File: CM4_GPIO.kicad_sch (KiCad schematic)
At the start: 21 parts, among them J4 Conn_02x07_Odd_Even, J5 Conn_01x03, J6 Conn_01x03, J7 THD-20-R, J8 Micro_SD_Card_Det, U4 74LVC1G07SE-7, U5 74LVC1G07SE-7, U6 RT9742GGJ5

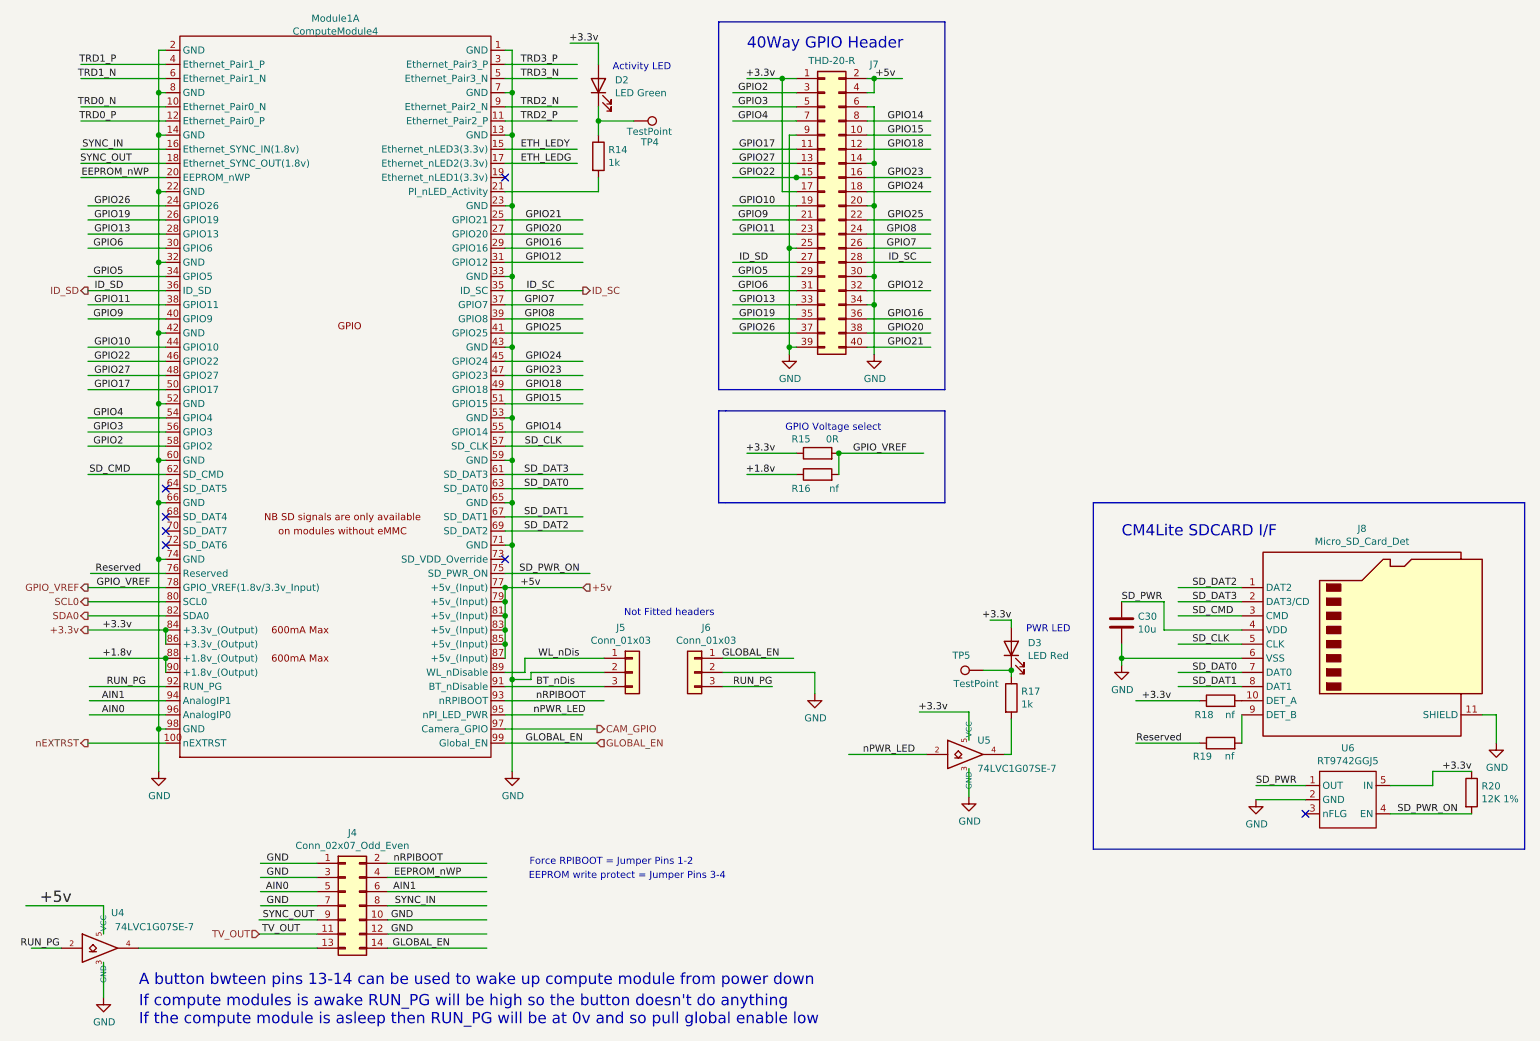
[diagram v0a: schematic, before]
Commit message: Initial layout and all parts added. Some pins still not connected to power
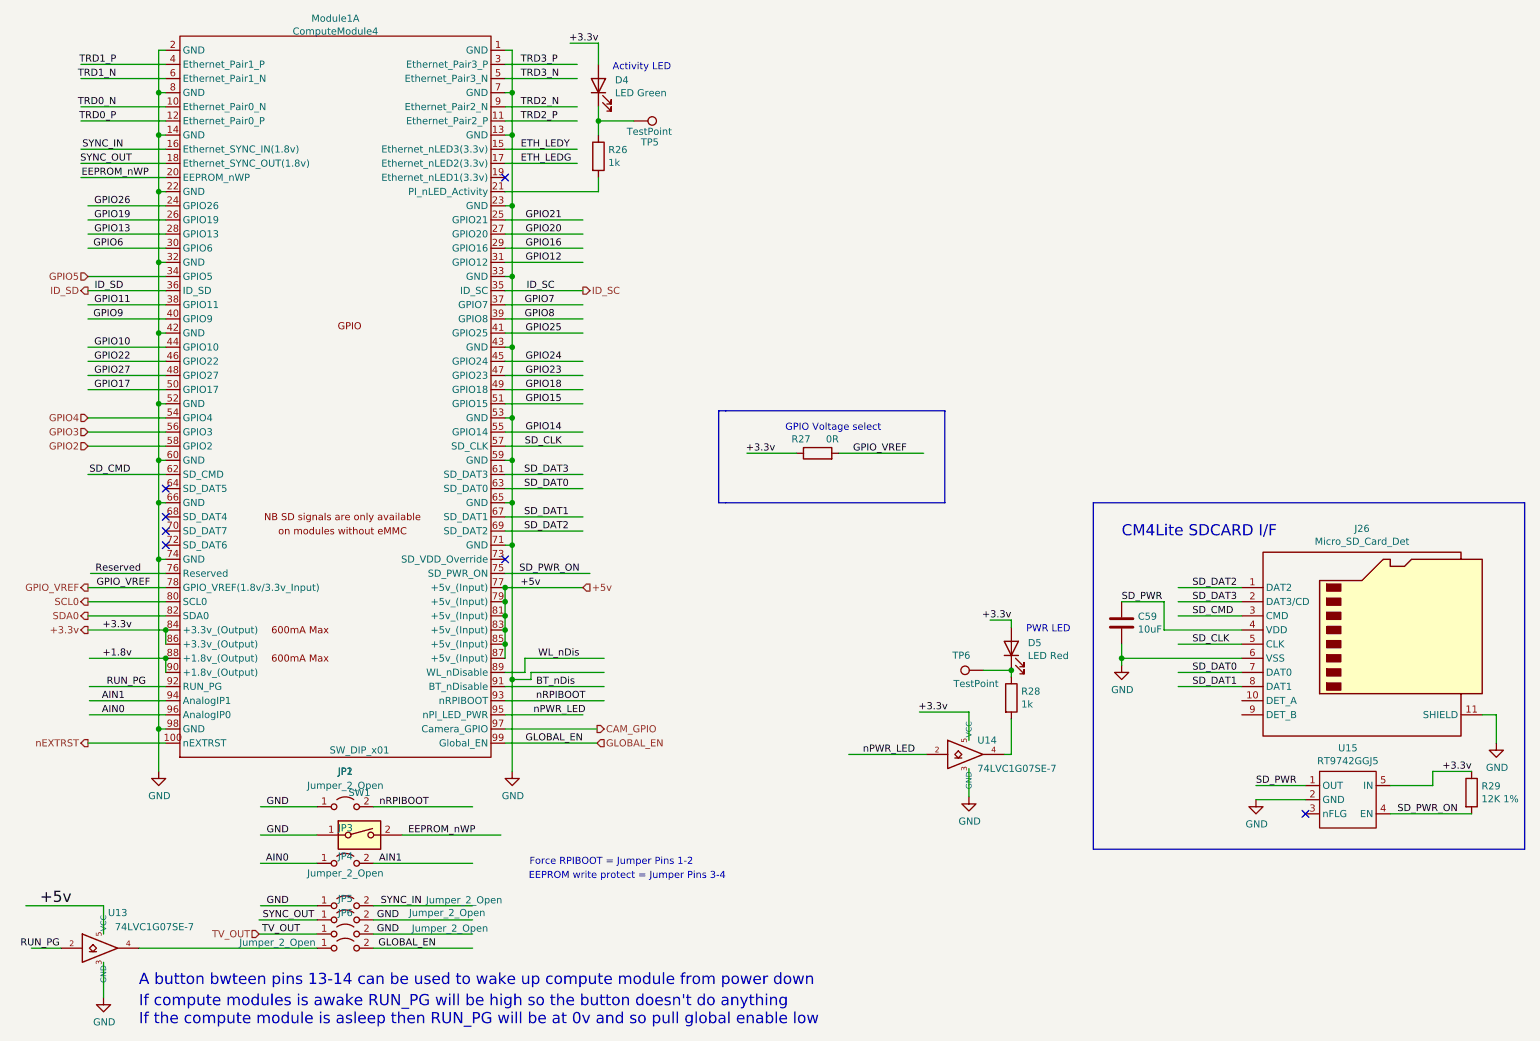
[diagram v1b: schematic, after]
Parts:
- removed J4: Conn_02x07_Odd_Even, Connector_PinHeader_2.54mm:PinHeader_2x07_P2.54mm_Vertical, symbol Connector_Generic:Conn_02x07_Odd_Even
- removed J5, J6: Conn_01x03, Connector_PinHeader_2.54mm:PinHeader_1x03_P2.54mm_Vertical, symbol Connector_Generic:Conn_01x03
- removed J7: THD-20-R, Connector_PinHeader_2.54mm:PinHeader_2x20_P2.54mm_Vertical, symbol Connector_Generic:Conn_02x20_Odd_Even
- removed R16, R18, R19: nf, Resistor_SMD:R_0402_1005Metric, symbol Device:R
- added JP1, JP2, JP3, JP4, JP5, JP6: Jumper_2_Open, Jumper:SolderJumper-2_P1.3mm_Open_RoundedPad1.0x1.5mm, symbol Jumper:Jumper_2_Open
- added SW1: SW_DIP_x01, Button_Switch_SMD:SW_DIP_SPSTx01_Slide_6.7x4.1mm_W8.61mm_P2.54mm_LowProfile, symbol Switch:SW_DIP_x01
- C59: renamed from C30; value 10u -> 10uF
- renumbered D2 to D4, D3 to D5, J8 to J26, R14 to R26, R15 to R27, R17 to R28, R20 to R29, TP4 to TP5, TP5 to TP6, U4 to U13, U5 to U14, U6 to U15
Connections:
- net AIN0: now also JP2.1 (A)
- net AIN1: now also JP2.2 (B)
- net EEPROM_nWP: now also SW1.2
- net GLOBAL_EN: now also JP6.2 (B)
- net GND: now also JP1.1 (A), JP3.1 (A), JP4.2 (B), JP5.2 (B), SW1.1
- net SYNC_IN: now also JP3.2 (B)
- net SYNC_OUT: now also JP4.1 (A)
- net TV_OUT: now also JP5.1 (A)
- net nRPIBOOT: now also JP1.2 (B)
- net at U13.4: now also JP6.1 (A)
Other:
- note removed: "40Way GPIO Header"
- note removed: "Not Fitted headers"

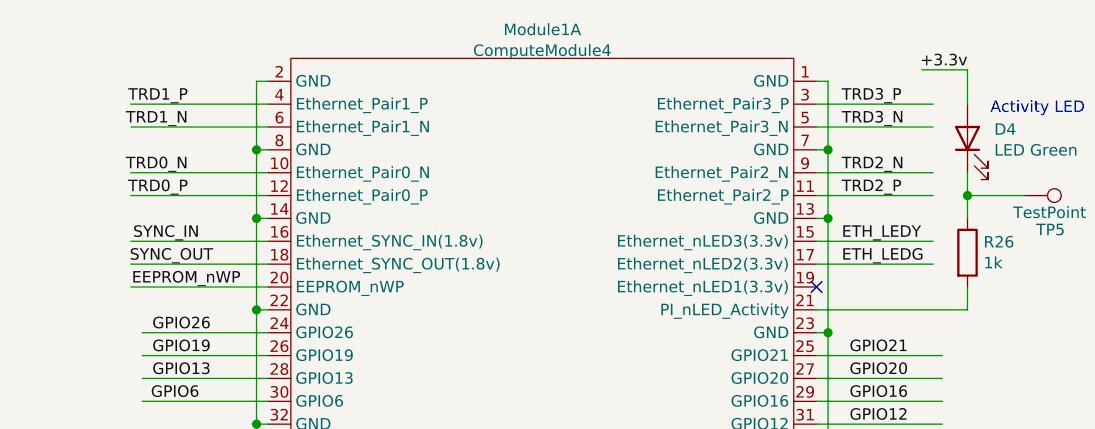
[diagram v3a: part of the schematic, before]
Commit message: Added usb to ethernet and changed mcu to stm32g4
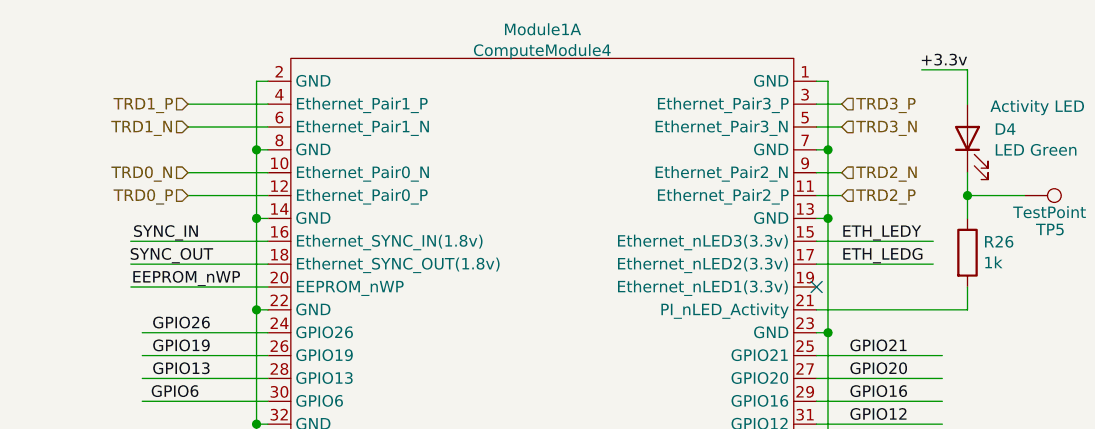
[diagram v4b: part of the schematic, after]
